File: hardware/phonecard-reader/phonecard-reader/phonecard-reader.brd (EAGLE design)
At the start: 62 x 78 mm, 2 parts

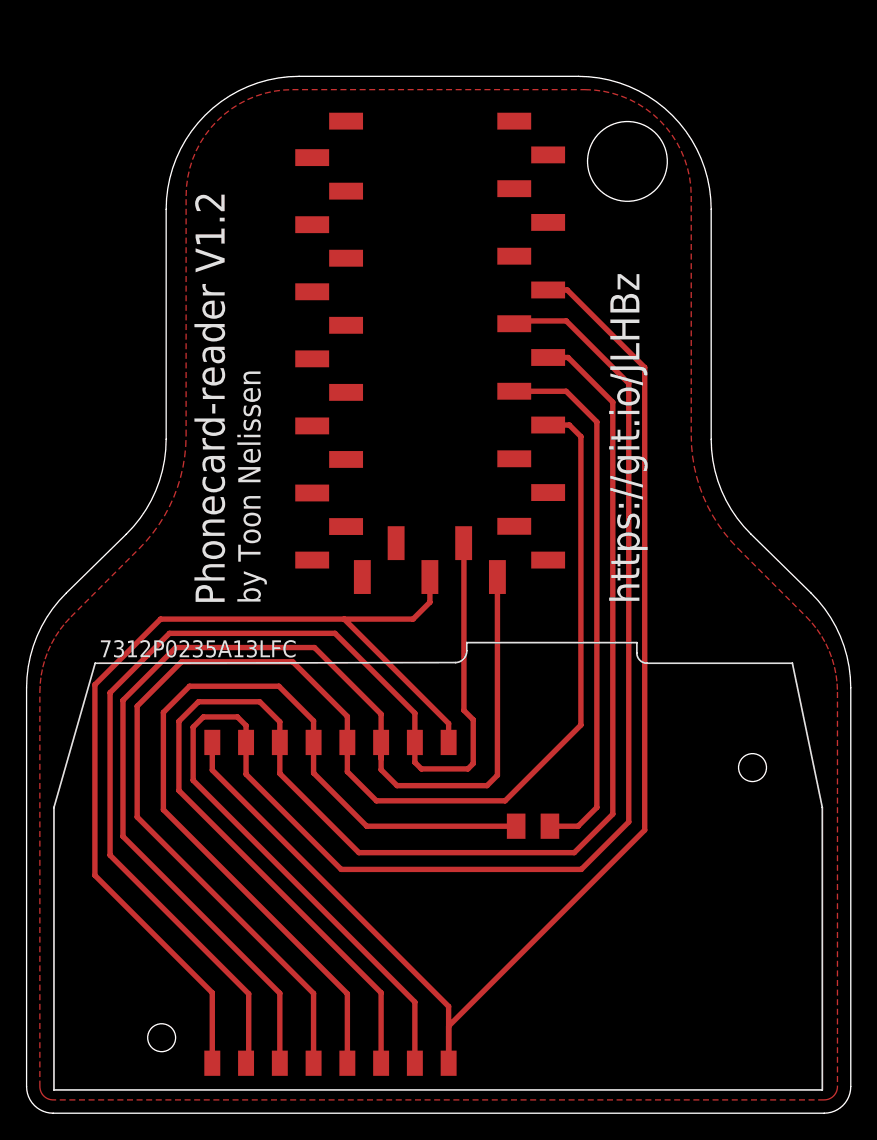
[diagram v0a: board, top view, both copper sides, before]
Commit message: feat: added azerty keyboard output jumper to pcb
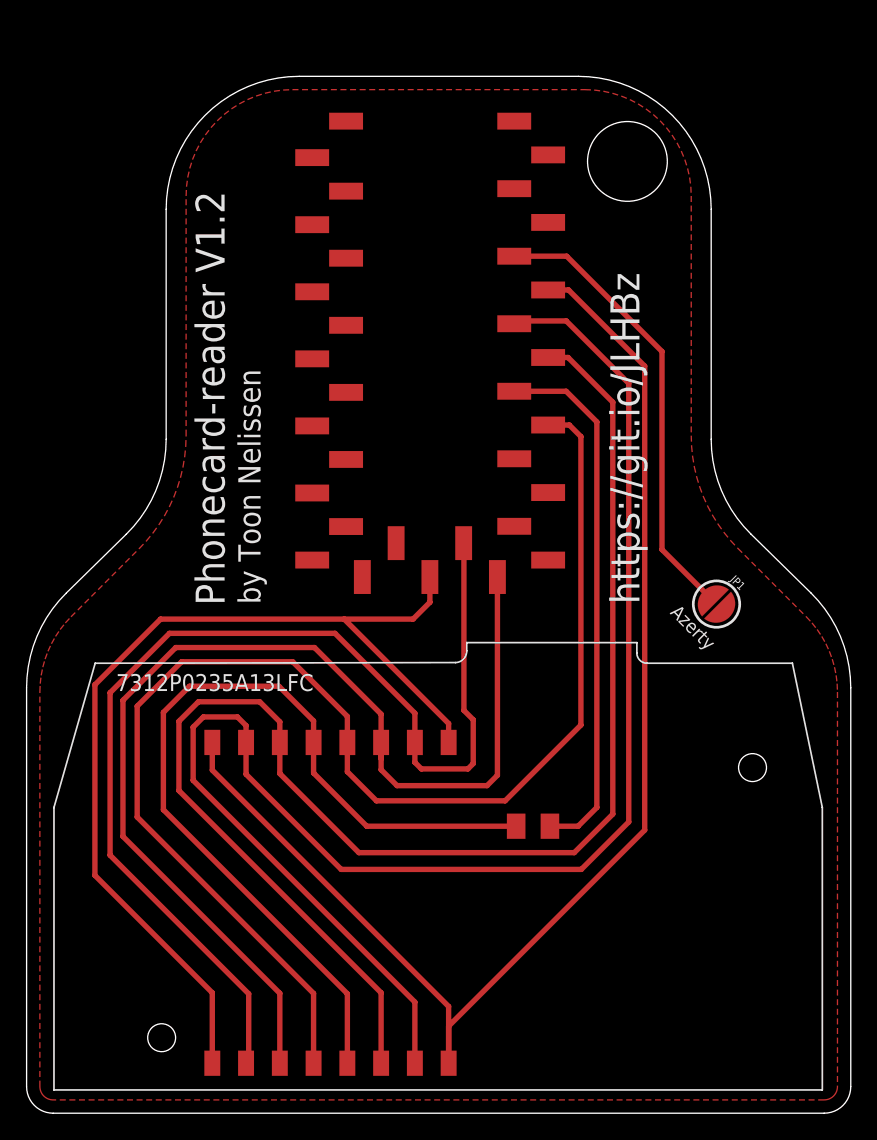
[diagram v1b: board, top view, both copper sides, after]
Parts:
- added JP1: Azerty, SparkFun-Jumpers:SMT-JUMPER_2_NO_SILK_ROUND
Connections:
- new net N$1: JP1.1, U$1.12
- net GND: now also JP1.2
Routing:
- net N$1: track 0.00 -> 33.7 mm

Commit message: feat: update keyboard switch pin
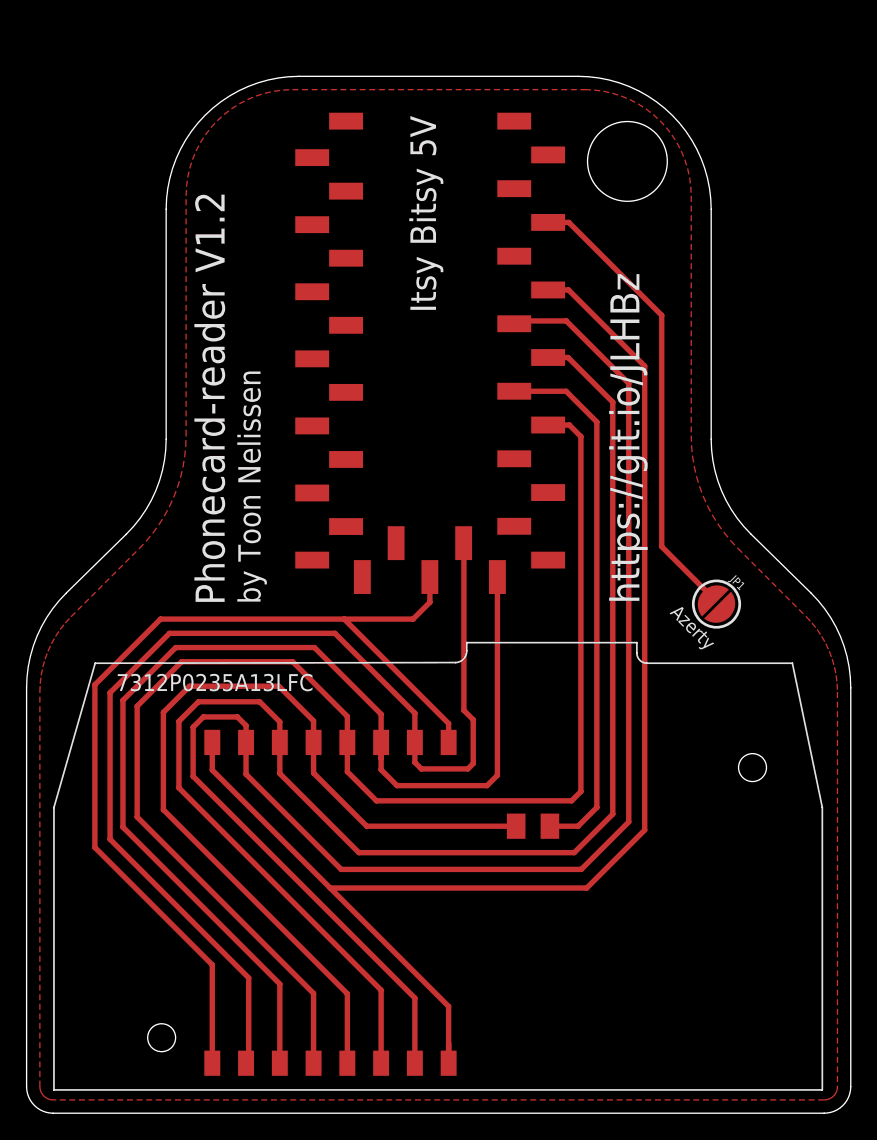
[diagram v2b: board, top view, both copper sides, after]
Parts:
- U$1: value (none) -> Itsy Bitsy 5V
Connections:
- net N$1: now also U$1.13; no longer U$1.12
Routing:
- net CARD8: track 99.7 -> 103.0 mm
- net CARD1: track 100.8 -> 103.7 mm
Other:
- board text added: "Itsy Bitsy 5V"
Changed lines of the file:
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@@
 <drawing>
 <settings>
-<setting alwaysvectorfont="yes"/>
+<setting alwaysvectorfont="no"/>
 <setting verticaltext="up"/>
 </settings>
@@
 <text x="17.6" y="38.3" size="1.6764" layer="25" font="vector" ratio="10" rot="R90">by Toon Nelissen</text>
 <text x="46.1" y="38.3" size="2.1844" layer="25" font="vector" ratio="13" rot="R90">https://git.io/JLHBz</text>
+<text x="30.8" y="60.2" size="1.9304" layer="25" rot="R90">Itsy Bitsy 5V</text>
 </plain>
 <attributes>
@@
 </autorouter>
 <elements>
-<element name="U$1" library="mylibrary" library_urn="urn:adsk.eagle:library:25379741" package="ITSY_BITSY_SMD" value="" x="37.96" y="41.61" smashed="yes" rot="R90"/>
+<element name="U$1" library="mylibrary" library_urn="urn:adsk.eagle:library:25379741" package="ITSY_BITSY_SMD" value="Itsy Bitsy 5V" x="37.96" y="41.61" smashed="yes" rot="R90"/>
 <element name="U$2" library="mylibrary" library_urn="urn:adsk.eagle:library:25379741" package="7312P0235A13" package3d_urn="urn:adsk.eagle:package:25379743/2" value="" x="54.61" y="26" smashed="yes"/>
 <element name="JP1" library="SparkFun-Jumpers" library_urn="urn:adsk.eagle:library:528" package="SMT-JUMPER_2_NO_SILK_ROUND" package3d_urn="urn:adsk.eagle:package:39280/1" value="Azerty" x="51.9" y="38.3" smashed="yes" rot="R315">
@@
 <wire x1="26.32" y1="23.5" x2="24.13" y2="25.69" width="0.4064" layer="1"/>
 <wire x1="24.13" y1="27.89" x2="24.13" y2="25.69" width="0.4064" layer="1"/>
-<wire x1="26.32" y1="23.5" x2="36" y2="23.5" width="0.4064" layer="1"/>
-<wire x1="36" y1="23.5" x2="41.7" y2="29.2" width="0.4064" layer="1"/>
-<wire x1="41.7" y1="29.2" x2="41.7" y2="50.9" width="0.4064" layer="1"/>
+<wire x1="26.32" y1="23.5" x2="41" y2="23.5" width="0.4064" layer="1"/>
+<wire x1="41" y1="23.5" x2="41.7" y2="24.2" width="0.4064" layer="1"/>
+<wire x1="41.7" y1="24.2" x2="41.7" y2="50.9" width="0.4064" layer="1"/>
 <wire x1="41.7" y1="50.9" x2="40.83" y2="51.77" width="0.4064" layer="1"/>
 <wire x1="40.83" y1="51.77" x2="39.235" y2="51.77" width="0.4064" layer="1"/>
@@
 </signal>
 <signal name="CARD2">
-<wire x1="19.05" y1="3.76" x2="19.05" y2="9.02" width="0.4064" layer="1"/>
-<wire x1="7.25" y1="20.82" x2="7.25" y2="31.06" width="0.4064" layer="1"/>
+<wire x1="19.05" y1="3.76" x2="19.05" y2="9.72" width="0.4064" layer="1"/>
+<wire x1="7.25" y1="21.52" x2="7.25" y2="31.06" width="0.4064" layer="1"/>
 <wire x1="7.25" y1="31.06" x2="11.22" y2="35.03" width="0.4064" layer="1"/>
 <wire x1="11.22" y1="35.03" x2="21.66" y2="35.03" width="0.4064" layer="1"/>
@@
 <wire x1="26.67" y1="30.02" x2="26.67" y2="27.89" width="0.4064" layer="1"/>
 <wire x1="26.67" y1="26.67" x2="26.67" y2="27.89" width="0.4064" layer="1"/>
-<wire x1="19.05" y1="9.02" x2="7.25" y2="20.82" width="0.4064" layer="1"/>
+<wire x1="19.05" y1="9.72" x2="7.25" y2="21.52" width="0.4064" layer="1"/>
 <contactref element="U$1" pad="4"/>
 <wire x1="26.67" y1="27.89" x2="26.67" y2="25.83973125" width="0.4064" layer="1"/>
@@
 <wire x1="23.2" y1="36.1" x2="10.75" y2="36.1" width="0.4064" layer="1"/>
 <wire x1="10.75" y1="36.1" x2="6.28" y2="31.63" width="0.4064" layer="1"/>
-<wire x1="6.28" y1="31.63" x2="6.28" y2="19.41" width="0.4064" layer="1"/>
-<wire x1="6.28" y1="19.41" x2="16.71" y2="8.98" width="0.4064" layer="1"/>
-<wire x1="16.71" y1="8.98" x2="16.71" y2="3.96" width="0.4064" layer="1"/>
+<wire x1="6.28" y1="31.63" x2="6.28" y2="20.61" width="0.4064" layer="1"/>
+<wire x1="6.28" y1="20.61" x2="16.71" y2="10.18" width="0.4064" layer="1"/>
+<wire x1="16.71" y1="10.18" x2="16.71" y2="3.96" width="0.4064" layer="1"/>
 <wire x1="16.71" y1="3.96" x2="16.51" y2="3.76" width="0.4064" layer="1"/>
 <wire x1="29.21" y1="27.89" x2="29.21" y2="26.39" width="0.4064" layer="1"/>
@@
 </signal>
 <signal name="CARD4">
-<wire x1="13.97" y1="3.76" x2="13.97" y2="9.06" width="0.4064" layer="1"/>
-<wire x1="13.97" y1="9.06" x2="5.14" y2="17.89" width="0.4064" layer="1"/>
-<wire x1="5.14" y1="17.89" x2="5.14" y2="32.23" width="0.4064" layer="1"/>
+<wire x1="13.97" y1="3.76" x2="13.97" y2="11.16" width="0.4064" layer="1"/>
+<wire x1="13.97" y1="11.16" x2="5.14" y2="19.99" width="0.4064" layer="1"/>
+<wire x1="5.14" y1="19.99" x2="5.14" y2="32.23" width="0.4064" layer="1"/>
 <wire x1="5.14" y1="32.23" x2="10.08" y2="37.17" width="0.4064" layer="1"/>
 <wire x1="23.8917125" y1="37.17" x2="31.75" y2="29.3117125" width="0.4064" layer="1"/>
@@
 <signal name="CARD6">
 <contactref element="U$1" pad="9"/>
-<wire x1="26.67" y1="9.06" x2="11.46" y2="24.27" width="0.4064" layer="1"/>
-<wire x1="11.46" y1="24.27" x2="11.46" y2="29.48" width="0.4064" layer="1"/>
+<wire x1="26.67" y1="9.26" x2="11.46" y2="24.47" width="0.4064" layer="1"/>
+<wire x1="11.46" y1="24.47" x2="11.46" y2="29.48" width="0.4064" layer="1"/>
 <wire x1="11.46" y1="29.48" x2="12.93" y2="30.95" width="0.4064" layer="1"/>
 <wire x1="17.54" y1="30.95" x2="19.05" y2="29.44" width="0.4064" layer="1"/>
 <wire x1="19.05" y1="29.44" x2="19.05" y2="27.89" width="0.4064" layer="1"/>
-<wire x1="26.67" y1="3.76" x2="26.67" y2="9.06" width="0.4064" layer="1"/>
+<wire x1="26.67" y1="3.76" x2="26.67" y2="9.26" width="0.4064" layer="1"/>
 <wire x1="12.93" y1="30.95" x2="17.54" y2="30.95" width="0.4064" layer="1"/>
 <wire x1="19.05" y1="27.89" x2="19.05" y2="25.55" width="0.4064" layer="1"/>
@@
 <signal name="CARD7">
 <contactref element="U$1" pad="10"/>
-<wire x1="29.21" y1="3.76" x2="29.21" y2="8.36" width="0.4064" layer="1"/>
-<wire x1="29.21" y1="8.36" x2="12.53" y2="25.04" width="0.4064" layer="1"/>
+<wire x1="29.21" y1="3.76" x2="29.21" y2="8.66" width="0.4064" layer="1"/>
+<wire x1="29.21" y1="8.66" x2="12.53" y2="25.34" width="0.4064" layer="1"/>
 <wire x1="12.53" y1="29.04" x2="13.3" y2="29.81" width="0.4064" layer="1"/>
 <wire x1="13.3" y1="29.81" x2="15.86" y2="29.81" width="0.4064" layer="1"/>
 <wire x1="16.51" y1="29.16" x2="15.86" y2="29.81" width="0.4064" layer="1"/>
 <wire x1="16.51" y1="29.16" x2="16.51" y2="27.89" width="0.4064" layer="1"/>
-<wire x1="12.53" y1="25.04" x2="12.53" y2="29.04" width="0.4064" layer="1"/>
+<wire x1="12.53" y1="25.34" x2="12.53" y2="29.04" width="0.4064" layer="1"/>
 <wire x1="23.66853125" y1="18.3412" x2="41.73146875" y2="18.3412" width="0.4064" layer="1"/>
 <wire x1="41.73146875" y1="18.3412" x2="45.3" y2="21.90973125" width="0.4064" layer="1"/>
@@
 <contactref element="U$1" pad="11"/>
 <wire x1="31.75" y1="3.76" x2="31.75" y2="8.03" width="0.4064" layer="1"/>
-<wire x1="31.75" y1="8.03" x2="13.97" y2="25.81" width="0.4064" layer="1"/>
+<wire x1="31.75" y1="8.03" x2="22.84" y2="16.94" width="0.4064" layer="1"/>
+<wire x1="22.84" y1="16.94" x2="13.97" y2="25.81" width="0.4064" layer="1"/>
 <wire x1="13.97" y1="25.81" x2="13.97" y2="27.87" width="0.4064" layer="1"/>
 <wire x1="46.5" y1="21.3" x2="46.5" y2="56.2" width="0.4064" layer="1"/>
 <wire x1="40.77" y1="61.93" x2="39.235" y2="61.93" width="0.4064" layer="1"/>
 <wire x1="46.5" y1="56.2" x2="40.77" y2="61.93" width="0.4064" layer="1"/>
-<wire x1="31.75" y1="3.76" x2="31.75" y2="6.55" width="0.4064" layer="1"/>
-<wire x1="46.5" y1="21.3" x2="31.75" y2="6.55" width="0.4064" layer="1"/>
+<wire x1="31.75" y1="3.76" x2="31.75" y2="5.26" width="0.4064" layer="1"/>
 <contactref element="U$2" pad="I8"/>
+<wire x1="46.5" y1="21.3" x2="42.14" y2="16.94" width="0.4064" layer="1"/>
+<wire x1="42.14" y1="16.94" x2="22.84" y2="16.94" width="0.4064" layer="1"/>
 <wire x1="13.97" y1="27.87" x2="13.97" y2="27.89" width="0" layer="19" extent="1-1"/>
 </signal>
@@
 </signal>
 <signal name="N$1">
-<contactref element="U$1" pad="12"/>
+<contactref element="U$1" pad="13"/>
 <contactref element="JP1" pad="1"/>
-<wire x1="36.685" y1="64.47" x2="40.63" y2="64.47" width="0.4064" layer="1"/>
-<wire x1="40.63" y1="64.47" x2="47.8" y2="57.3" width="0.4064" layer="1"/>
-<wire x1="47.8" y1="42.4" x2="51.1" y2="39.1" width="0.4064" layer="1"/>
-<wire x1="47.8" y1="57.3" x2="47.8" y2="42.4" width="0.4064" layer="1"/>
-<wire x1="51.1" y1="39.1" x2="51.001971875" y2="39.198025" width="0" layer="19" extent="1-1"/>
+<wire x1="39.235" y1="67.01" x2="40.79" y2="67.01" width="0.4064" layer="1"/>
+<wire x1="40.79" y1="67.01" x2="47.780803125" y2="60.019196875" width="0.4064" layer="1"/>
+<wire x1="47.780803125" y1="42.619196875" x2="51.3" y2="39.1" width="0.4064" layer="1"/>
+<wire x1="47.780803125" y1="60.019196875" x2="47.780803125" y2="42.619196875" width="0.4064" layer="1"/>
+<wire x1="51.3" y1="39.1" x2="51.001971875" y2="39.198025" width="0" layer="19" extent="1-1"/>
 </signal>
 </signals>
